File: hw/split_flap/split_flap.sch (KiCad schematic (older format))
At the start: 8 parts, among them J15 MOTOR_POWER, J16 JUMPER_MOTOR_5V, J17 EXPANDER_PORT, J19 POWER, U1 74HCT125, U2 NodeMCU_1.0_(ESP-12E)

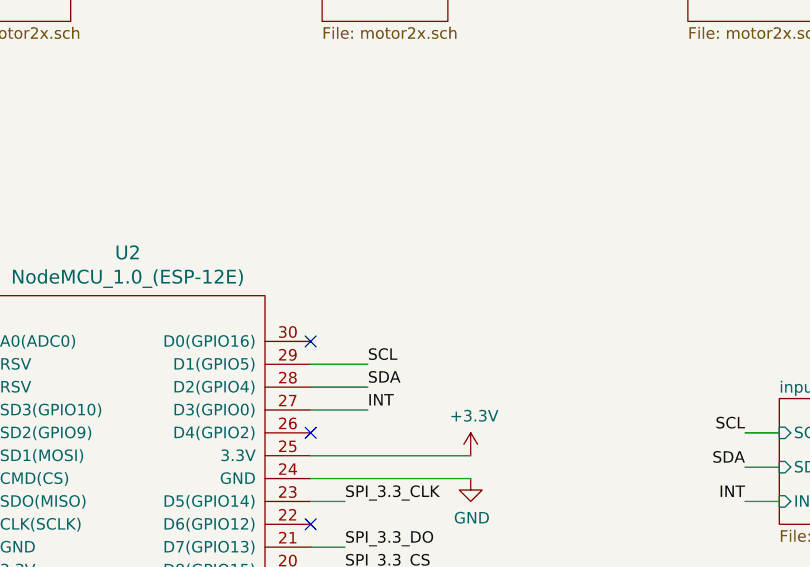
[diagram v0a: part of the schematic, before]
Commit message: Add i2c pullups
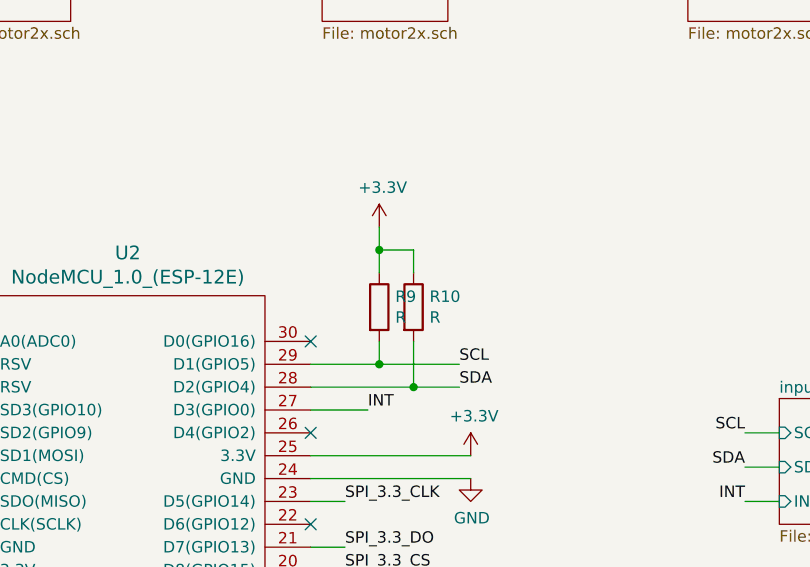
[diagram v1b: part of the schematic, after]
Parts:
- added R10, R9: R, Resistor_THT:R_Axial_DIN0207_L6.3mm_D2.5mm_P10.16mm_Horizontal, symbol Device:R
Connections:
- net +3V3: now also R10.1, R9.1
- net SCL: now also R9.2
- net SDA: now also R10.2
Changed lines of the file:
@@
 Text Label 3400 4050 0    50   ~ 0
 INT
-Text Label 3400 3950 0    50   ~ 0
+Text Label 3800 3950 0    50   ~ 0
 SDA
-Text Label 3400 3850 0    50   ~ 0
+Text Label 3800 3850 0    50   ~ 0
 SCL
 Wire Wire Line
-	3150 3850 3400 3850
-Wire Wire Line
-	3400 3950 3150 3950
+	3150 3850 3450 3850
+Wire Wire Line
+	3800 3950 3600 3950
 Wire Wire Line
 	3150 4050 3400 4050
@@
 Wire Wire Line
 	9350 4150 9700 4150
+$Comp
+L Device:R R9
+U 1 1 5DFB5E58
+P 3450 3600
+F 0 "R9" H 3520 3646 50  0000 L CNN
+F 1 "R" H 3520 3555 50  0000 L CNN
+F 2 "Resistor_THT:R_Axial_DIN0207_L6.3mm_D2.5mm_P10.16mm_Horizontal" V 3380 3600 50  0001 C CNN
+F 3 "~" H 3450 3600 50  0001 C CNN
+	1    3450 3600
+	1    0    0    -1
+$EndComp
+$Comp
+L Device:R R10
+U 1 1 5DFBFF10
+P 3600 3600
+F 0 "R10" H 3670 3646 50  0000 L CNN
+F 1 "R" H 3670 3555 50  0000 L CNN
+F 2 "Resistor_THT:R_Axial_DIN0207_L6.3mm_D2.5mm_P10.16mm_Horizontal" V 3530 3600 50  0001 C CNN
+F 3 "~" H 3600 3600 50  0001 C CNN
+	1    3600 3600
+	1    0    0    -1
+$EndComp
+Wire Wire Line
+	3450 3750 3450 3850
+Connection ~ 3450 3850
+Wire Wire Line
+	3450 3850 3800 3850
+Wire Wire Line
+	3600 3950 3600 3750
+Connection ~ 3600 3950
+Wire Wire Line
+	3600 3950 3150 3950
+$Comp
+L power:+3.3V #PWR071
+U 1 1 5DFC4BEF
+P 3450 3250
+F 0 "#PWR071" H 3450 3100 50  0001 C CNN
+F 1 "+3.3V" H 3465 3423 50  0000 C CNN
+F 2 "" H 3450 3250 50  0001 C CNN
+F 3 "" H 3450 3250 50  0001 C CNN
+	1    3450 3250
+	1    0    0    -1
+$EndComp
+Wire Wire Line
+	3450 3250 3450 3350
+Wire Wire Line
+	3450 3350 3600 3350
+Wire Wire Line
+	3600 3350 3600 3450
+Connection ~ 3450 3350
+Wire Wire Line
+	3450 3350 3450 3450
 $EndSCHEMATC
